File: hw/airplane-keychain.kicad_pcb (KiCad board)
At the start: 2 copper layers, 93.7 x 109.7 mm, 26 parts, among them SW1 SW_PUSH, SW2 SPST, U1 ATtiny85-20P

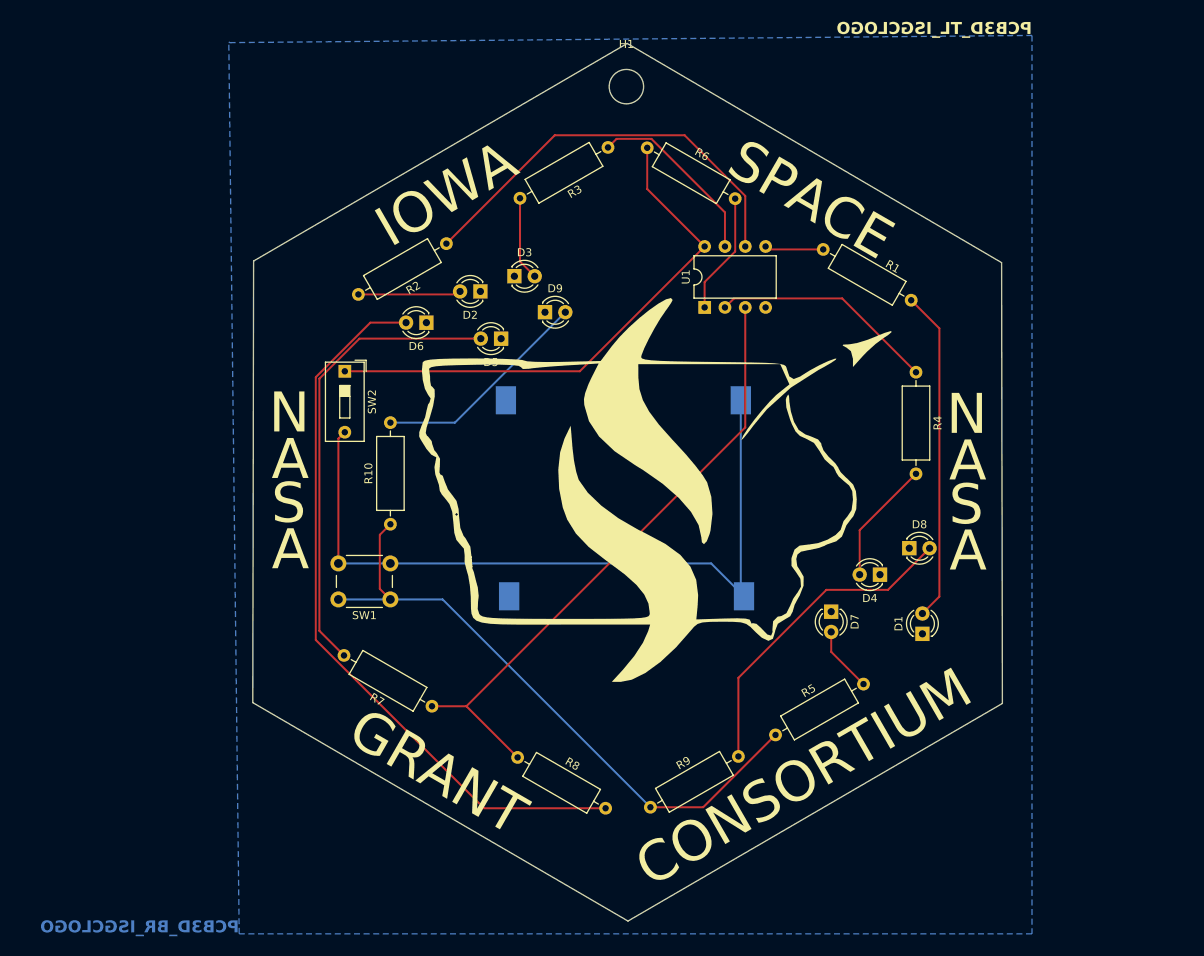
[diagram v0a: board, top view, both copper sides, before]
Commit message: Rev B
Removed some components
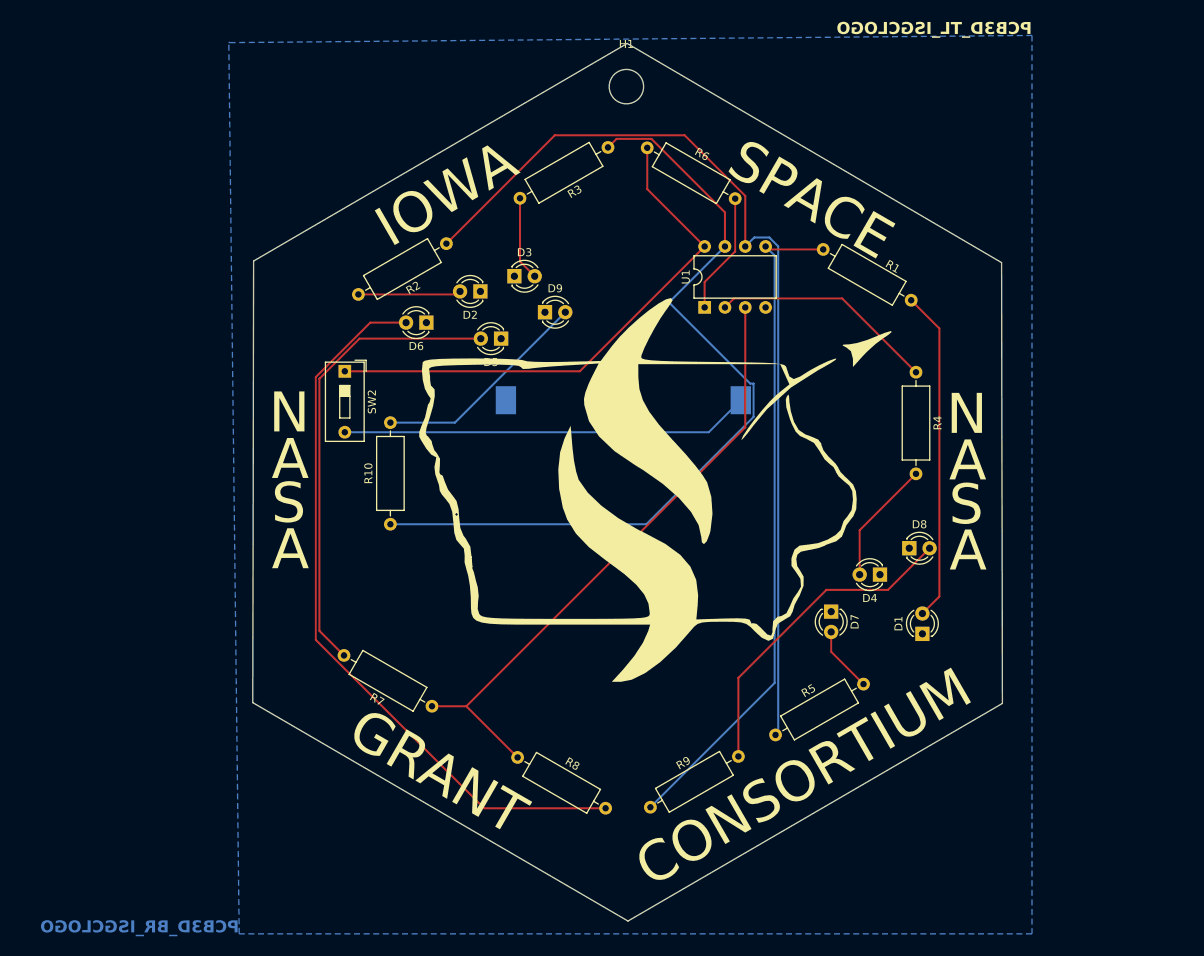
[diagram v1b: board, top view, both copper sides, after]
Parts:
- removed BT2: Battery_Cell, Battery:BatteryHolder_Keystone_1058_1x2032
- removed SW1: SW_PUSH, Button_Switch_THT:SW_PUSH_6mm
- R1, R10, R2, R3, R4, R5, R7, R8, R9: value 100 -> 120
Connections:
- R10 pad 1: Net-(R10-Pad1) -> Net-(U1-PB2)
- R5 pad 1: Net-(R10-Pad1) -> Net-(U1-PB1)
- R9 pad 1: Net-(R10-Pad1) -> Net-(U1-AREF/PB0)
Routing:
- net Net-(U1-PB2): track 23.1 -> 102.9 mm
- net Net-(R10-Pad1): track 79.6 -> 0.00 mm
- net Net-(U1-AREF/PB0): track 7.35 -> 84.3 mm
- net Net-(U1-PB1): track 52.4 -> 118.7 mm
- net Net-(BT1-+): track 94.8 -> 51.7 mm
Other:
- board text added: "ISGC Badge Rev B Matthew E. Nelson"
- board text removed: "ISGC Badge Rev A Matthew E. Nelson"

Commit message: draft
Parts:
- removed D7, D8, D9: LED, LED_THT:LED_D3.0mm
- removed R10, R5, R9: 120, Resistor_THT:R_Axial_DIN0309_L9.0mm_D3.2mm_P12.70mm_Horizontal
- moved D6 73.9 mm to (179.2, 84.0), turned to 0 degrees
- moved SW2 71.3 mm to (166.8, 86.5), turned to 180 degrees
- moved R8 66.3 mm to (181.2, 113.0), turned to 0 degrees
- moved D5 65.0 mm to (179.5, 68.9), turned to 0 degrees
- moved D1 64.8 mm to (189.7, 54.0), turned to 0 degrees
- moved R7 60.2 mm to (165.7, 113.0), turned to 0 degrees
- moved D2 59.9 mm to (148.7, 120.0), turned to 0 degrees
- moved R3 59.5 mm to (119.3, 113.0), turned to 0 degrees
- moved R2 47.0 mm to (104.2, 113.0), turned to 0 degrees
- moved R1 46.3 mm to (150.3, 113.0), turned to 0 degrees
- moved R4 44.5 mm to (134.8, 113.0), turned to 0 degrees
- moved D4 30.9 mm to (142.6, 84.0), turned to 0 degrees
- moved D3 25.9 mm to (142.7, 69.0)
- moved G*** 22.4 mm to (150.5, 85.5)
- moved H1 20.8 mm to (150.0, 54.5)
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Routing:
- net Net-(D6-A): track 91.9 -> 34.0 mm
- net Net-(D8-A): track 40.4 -> 0.00 mm
- net Net-(D3-A): track 10.5 -> 49.5 mm
- net Net-(U1-VCC): track 66.7 -> 32.4 mm
- net Net-(D1-A): track 41.5 -> 71.1 mm
- net Net-(D9-A): track 27.6 -> 0.00 mm
- net Net-(U1-PB2): track 102.9 -> 76.6 mm
- net Net-(D2-A): track 12.9 -> 37.3 mm
- net Net-(U1-PB1): track 118.7 -> 94.3 mm
- net Net-(U1-XTAL1/PB3): track 28.2 -> 51.3 mm
- net Net-(BT1-+): track 51.7 -> 71.2 mm, vias 0 -> 1
- net Net-(U1-XTAL2/PB4): track 77.6 -> 58.3 mm
- net Net-(U1-AREF/PB0): track 84.3 -> 67.6 mm
- net Net-(D4-A): track 15.5 -> 30.0 mm
- net Net-(D5-A): track 58.1 -> 45.6 mm
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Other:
- board size 93.7 x 109.7 mm -> 100 x 75 mm
- board text added: "Spring 2025"
- board text removed: "ISGC Badge Rev B Matthew E. Nelson"
- board text removed: "PCB3D_BR_ISGCLOGO"
- board text removed: "PCB3D_TL_ISGCLOGO"

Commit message: M2I Badge first run
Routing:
- net Net-(U1-PB1): track 94.3 -> 100.3 mm
- net Net-(BT1-+): track 71.2 -> 67.1 mm
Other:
- board text added: "Spring 2025 Awardee"
- board text removed: "Spring 2025"

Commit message: Production Run
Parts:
- D1, D3, D4: value LED -> Red; footprint LED_THT:LED_D3.0mm -> LED_SMD:LED_1206_3216Metric
- D2, D5, D6: value LED -> Amber; footprint LED_THT:LED_D3.0mm -> LED_SMD:LED_1206_3216Metric
- R1, R2, R3, R4, R6, R7, R8: footprint Resistor_THT:R_Axial_DIN0309_L9.0mm_D3.2mm_P12.70mm_Horizontal -> Resistor_SMD:R_1206_3216Metric
- moved R2 35.1 mm to (136.2, 98.7)
- moved BT1 32.5 mm to (150.8, 80.4)
- moved R3 27.5 mm to (142.7, 98.7)
- moved R4 26.3 mm to (156.8, 98.7)
- moved R1 24.8 mm to (130.0, 98.7)
- moved SW2 24.1 mm to (154.5, 65.7)
- moved D1 23.5 mm to (170.6, 67.6)
- moved D2 21.3 mm to (149.7, 98.7)
- moved R8 18.3 mm to (169.7, 98.7)
- moved U1 17.4 mm to (139.5, 71.5), turned to 180 degrees
- moved D5 16.0 mm to (165.1, 75.9), turned to 90 degrees
- moved R7 14.6 mm to (163.2, 98.6)
- moved D6 14.1 mm to (165.1, 83.6), turned to 90 degrees
- moved D3 8.13 mm to (146.7, 76.1), turned to -90 degrees
- moved R6 8.05 mm to (143.1, 61.3), turned to 180 degrees
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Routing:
- net Net-(U1-PB1): track 100.3 -> 34.8 mm
- net Net-(BT1-+): track 67.1 -> 20.9 mm
- net Net-(U1-PB2): track 76.6 -> 34.6 mm
- net GND: track 0.33 -> 31.9 mm, vias 0 -> 4
- net Net-(U1-AREF/PB0): track 67.6 -> 36.2 mm
- net Net-(D3-A): track 49.5 -> 25.9 mm, vias 0 -> 2
- net Net-(D2-A): track 37.3 -> 14.4 mm
- net Net-(D5-A): track 45.6 -> 24.9 mm
- net Net-(D6-A): track 34.0 -> 19.0 mm
- net Net-(U1-XTAL1/PB3): track 51.3 -> 36.3 mm
- net Net-(U1-XTAL2/PB4): track 58.3 -> 48.8 mm
- net Net-(D4-A): track 30.0 -> 21.3 mm
- net Net-(U1-~{RESET}/PB5): track 7.01 -> 12.7 mm
- net Net-(D1-A): track 71.1 -> 73.8 mm
- net Net-(U1-VCC): track 32.4 -> 33.5 mm
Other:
- board size 100 x 75 mm -> 60 x 60 mm
- board text added: "Fall 2025 Awardee"
- board text removed: "Spring 2025 Awardee"

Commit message: Minor change for S26
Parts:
- added G***: LOGO, lib:pcbtree, B.Cu at (150.1, 100.3)
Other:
- board text added: "Docendo Discimus"
- board text added: "Innovate, Build, Launch"
- board text added: "Kaizen 改善"
- board text added: "Semper Discens"
- board text removed: "Fall 2025 Awardee"
